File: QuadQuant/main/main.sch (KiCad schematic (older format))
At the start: 30 parts, among them J1 USB_B_Mini, J2 Conn_02x05_Odd_Even, U1 LM7805_TO220, U2 ATmega32U4-AU, U3 MCP4728, Y1 Crystal16mhz

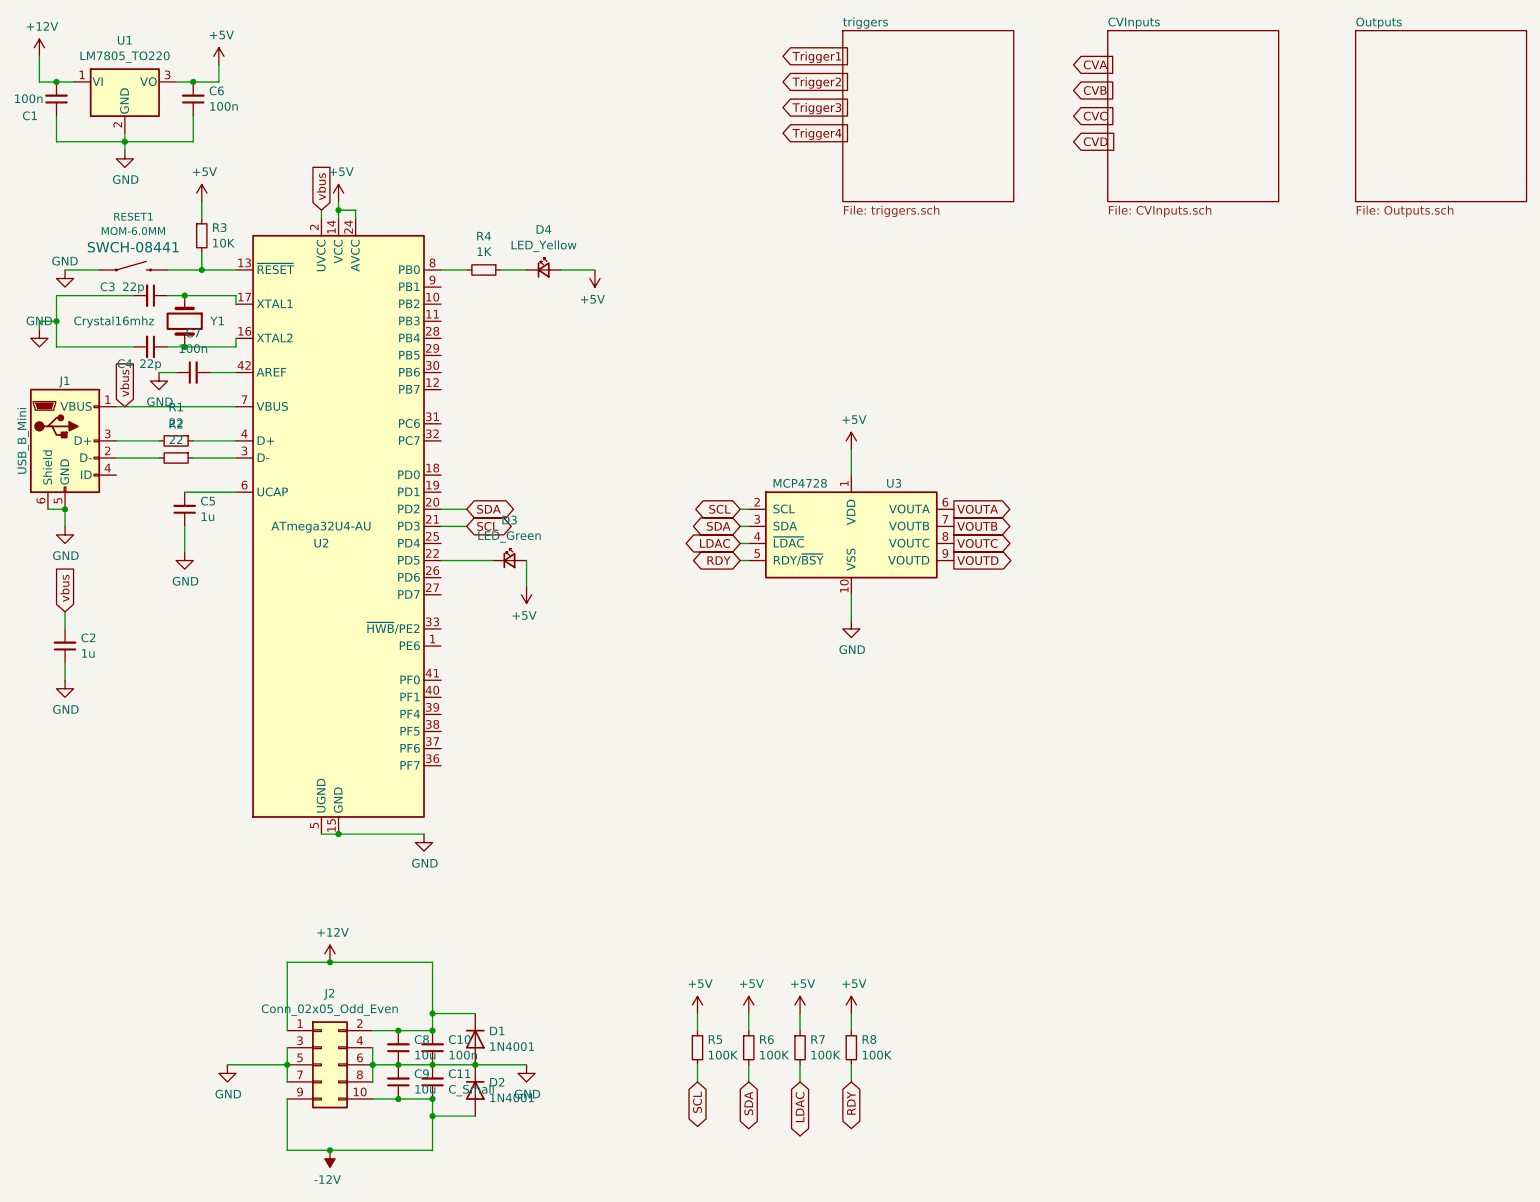
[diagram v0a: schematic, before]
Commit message: Adding programming headers
Also starting in on a PCB layout. My smd work is so fugly right now.
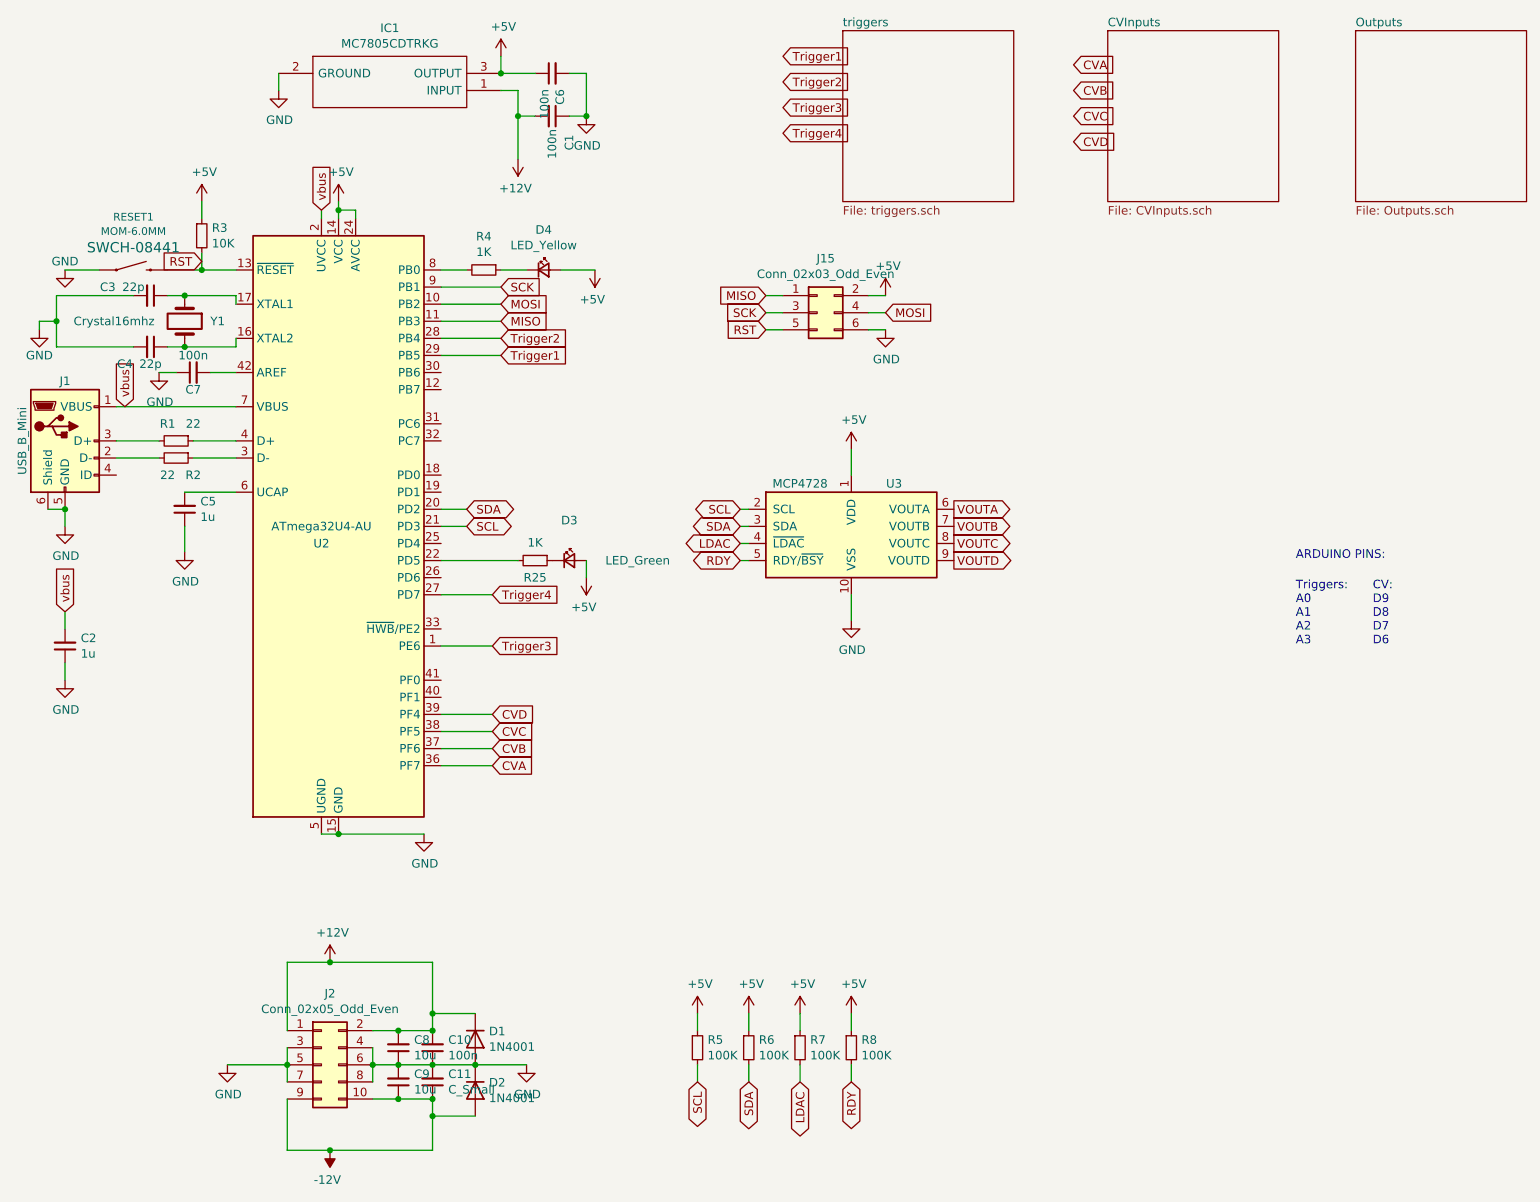
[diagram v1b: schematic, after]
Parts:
- removed U1: LM7805_TO220, Package_TO_SOT_THT:TO-220-3_Vertical, symbol Regulator_Linear:LM7805_TO220
- added IC1: MC7805CDTRKG, SamacSys_Parts:MJD1221G, symbol SamacSys_Parts:MC7805CDTRKG
- added J15: Conn_02x03_Odd_Even, Connector_PinSocket_2.54mm:PinSocket_2x03_P2.54mm_Vertical, symbol Connector_Generic:Conn_02x03_Odd_Even
- added R25: 1K, Resistor_SMD:R_0805_2012Metric, symbol Device:R_Small
- J2: footprint Connector_PinHeader_1.27mm:PinHeader_2x05_P1.27mm_Vertical -> Connector_PinSocket_2.54mm:PinSocket_2x05_P2.54mm_Vertical
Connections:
- net +12V: now also IC1.1 (INPUT)
- net +5V: now also C6.1, IC1.3 (OUTPUT), J15.2 (Pin_2); no longer C6.2
- net CVA: now also U2.36 (PF7)
- net CVB: now also U2.37 (PF6)
- net CVC: now also U2.38 (PF5)
- net CVD: now also U2.39 (PF4)
- net GND: now also C6.2, IC1.2 (GROUND), J15.6 (Pin_6); no longer C6.1
- net Trigger1: now also U2.29 (PB5)
- net Trigger2: now also U2.28 (PB4)
- net Trigger3: now also U2.1 (PE6)
- net Trigger4: now also U2.27 (PD7)
- net MOSI: now reaches U2.10 (PB2)
- net MOSI: now also J15.4 (Pin_4)
- net MISO: now reaches U2.11 (PB3)
- net MISO: now also J15.1 (Pin_1)
- net RST: now reaches R3.2, RESET1.3 (2), U2.13 (~RESET)
- net RST: now also J15.5 (Pin_5)
- net at U2.22 (PD5): now also R25.2; no longer D3.1 (K)
- net SCK: now reaches U2.9 (PB1)
- net SCK: now also J15.3 (Pin_3)
- new net: D3.1 (K), R25.1
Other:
- note added: "ARDUINO PINS:"
- note added: "CV:\nD9\nD8\nD7\nD6"
- note added: "Triggers:\nA0\nA1\nA2\nA3"
- moved on the sheet: C1, D3
